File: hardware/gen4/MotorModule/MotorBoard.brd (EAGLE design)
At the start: 34 x 61.7 mm, 67 parts, among them IC1 XMEGA16A4A, M1O1 TEST_PT, M1O2 TEST_PT, M1O3 TEST_PT

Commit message: cleaned up a few things
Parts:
- R12, R13, R14: value 0 -> 240
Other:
- outline, holes or cut-outs redrawn
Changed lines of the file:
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@@
 <plain>
 <wire x1="-1" y1="-16.65875" x2="-1" y2="45" width="0.4064" layer="20"/>
-<wire x1="-1" y1="45" x2="33" y2="44.865" width="0.4064" layer="20"/>
-<wire x1="33" y1="44.865" x2="33" y2="-16.65875" width="0.4064" layer="20"/>
+<wire x1="-1" y1="45" x2="33" y2="45.02375" width="0.4064" layer="20"/>
+<wire x1="33" y1="45.02375" x2="33" y2="-16.65875" width="0.4064" layer="20"/>
 <wire x1="33" y1="-16.65875" x2="-1" y2="-16.65875" width="0.4064" layer="20"/>
 <text x="0.533125" y="45.761875" size="1.016" layer="21">Priorities:
 1. don't catch on fire
 2. play soccer</text>
+<dimension x1="33" y1="44.865" x2="33" y2="-16.65875" x3="46.19625" y3="14.103125" textsize="1.778" layer="20"/>
+<dimension x1="-1" y1="45" x2="33" y2="44.865" x3="16.074" y3="63.56980625" textsize="1.778" layer="20"/>
 </plain>
 <attributes>
@@
 <element name="R8" library="SparkFun-Resistors" package="0805" value="240" x="10.6875" y="32.8753125" rot="R180"/>
 <element name="R10" library="SparkFun-Resistors" package="0805" value="240" x="12.7" y="40.3225" rot="R180"/>
-<element name="R12" library="SparkFun-Resistors" package="0805" value="0" x="30.63875" y="22.70125" rot="R180"/>
-<element name="R13" library="SparkFun-Resistors" package="0805" value="0" x="28.2575" y="32.7025" rot="R180"/>
-<element name="R14" library="SparkFun-Resistors" package="0805" value="0" x="28.41625" y="40.9575" rot="R180"/>
+<element name="R12" library="SparkFun-Resistors" package="0805" value="240" x="30.63875" y="22.70125" rot="R180"/>
+<element name="R13" library="SparkFun-Resistors" package="0805" value="240" x="28.2575" y="32.7025" rot="R180"/>
+<element name="R14" library="SparkFun-Resistors" package="0805" value="240" x="28.41625" y="40.9575" rot="R180"/>
 <element name="R78" library="SparkFun-Resistors" package="0805" value="1k" x="21.74875" y="7.77875" rot="R90"/>
 <element name="R79" library="SparkFun-Resistors" package="0805" value="1k" x="21.74875" y="4.7625" rot="R90"/>

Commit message: motor board fix
final changes
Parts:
- R12, R13, R14: value 240 -> 0
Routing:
- net PWM1: track 49.3 -> 49.9 mm
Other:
- outline, holes or cut-outs redrawn

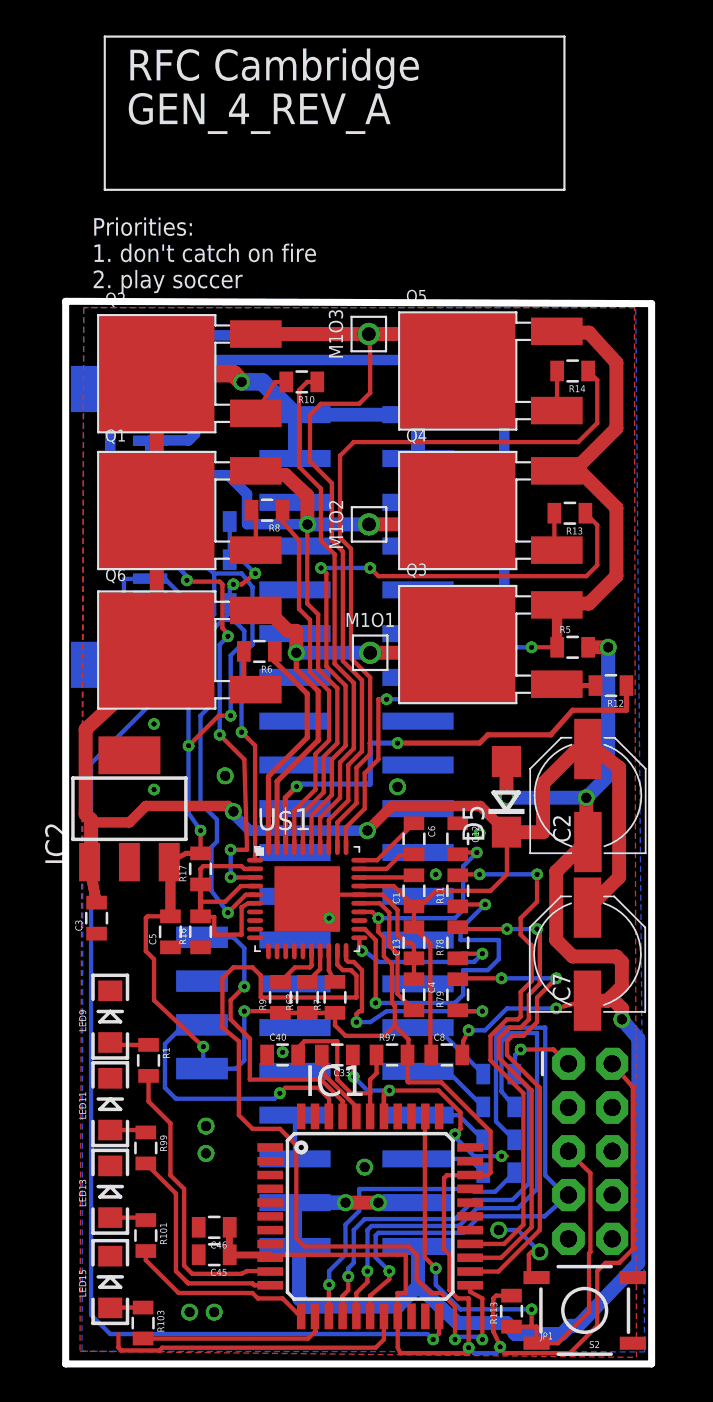
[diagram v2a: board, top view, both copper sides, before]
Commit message: motor and kicker fixes
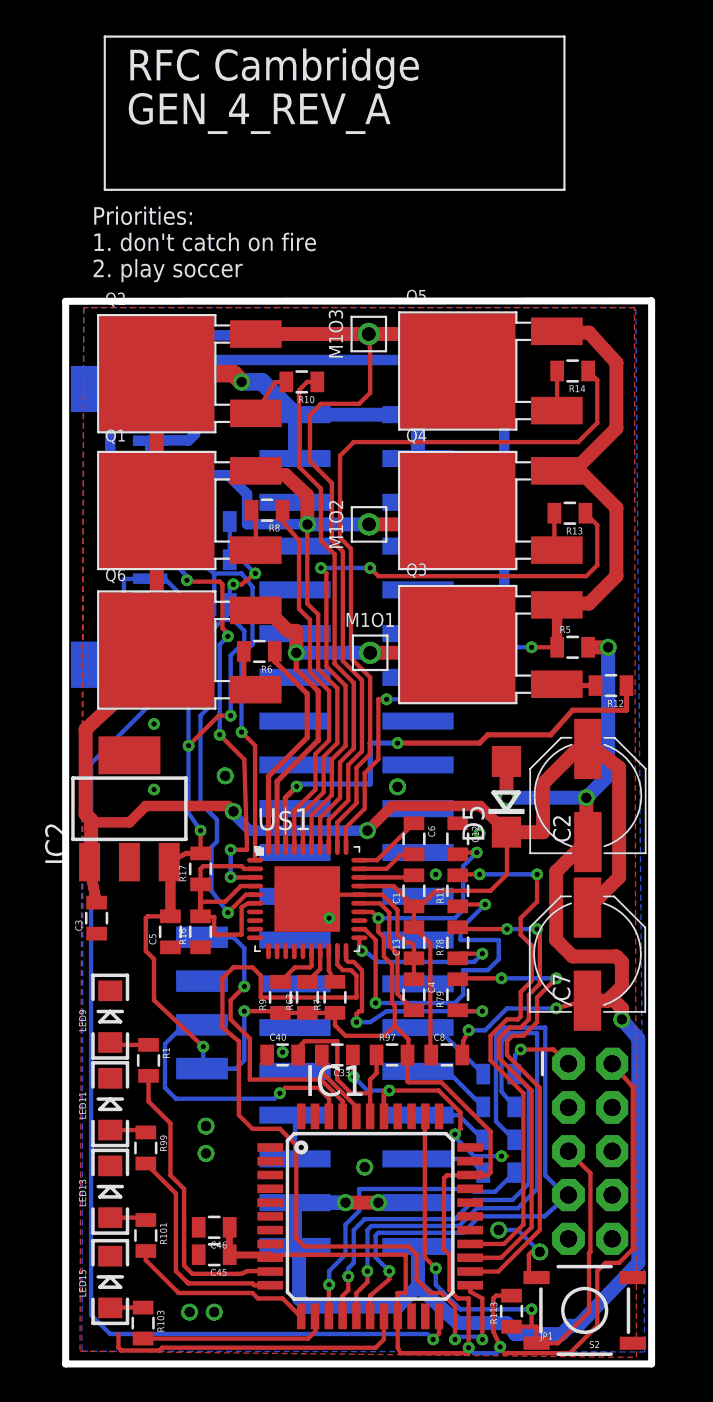
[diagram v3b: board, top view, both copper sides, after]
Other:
- outline, holes or cut-outs redrawn
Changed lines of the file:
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@@
 <plain>
 <wire x1="-1" y1="-16.65875" x2="-1" y2="45" width="0.4064" layer="20"/>
-<wire x1="-1" y1="45" x2="33" y2="44.865" width="0.4064" layer="20"/>
-<wire x1="33" y1="44.865" x2="33" y2="-16.65875" width="0.4064" layer="20"/>
+<wire x1="-1" y1="45" x2="33" y2="45.02375" width="0.4064" layer="20"/>
+<wire x1="33" y1="45.02375" x2="33" y2="-16.65875" width="0.4064" layer="20"/>
 <wire x1="33" y1="-16.65875" x2="-1" y2="-16.65875" width="0.4064" layer="20"/>
-<text x="0.533125" y="45.761875" size="1.016" layer="21">Priorities:
+<text x="0.533125" y="46.396875" size="1.016" layer="21">Priorities:
 1. don't catch on fire
 2. play soccer</text>

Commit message: motor layout stuff
idea: maybe moving some more stuff to the bottom would be beneficial
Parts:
- R12, R13, R14: value 0 -> 240
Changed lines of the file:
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@@
 <element name="R8" library="SparkFun-Resistors" package="0805" value="240" x="10.6875" y="32.8753125" rot="R180"/>
 <element name="R10" library="SparkFun-Resistors" package="0805" value="240" x="12.7" y="40.3225" rot="R180"/>
-<element name="R12" library="SparkFun-Resistors" package="0805" value="0" x="30.63875" y="22.70125" rot="R180"/>
-<element name="R13" library="SparkFun-Resistors" package="0805" value="0" x="28.2575" y="32.7025" rot="R180"/>
-<element name="R14" library="SparkFun-Resistors" package="0805" value="0" x="28.41625" y="40.9575" rot="R180"/>
+<element name="R12" library="SparkFun-Resistors" package="0805" value="240" x="30.63875" y="22.70125" rot="R180"/>
+<element name="R13" library="SparkFun-Resistors" package="0805" value="240" x="28.2575" y="32.7025" rot="R180"/>
+<element name="R14" library="SparkFun-Resistors" package="0805" value="240" x="28.41625" y="40.9575" rot="R180"/>
 <element name="R78" library="SparkFun-Resistors" package="0805" value="1k" x="21.74875" y="7.77875" rot="R90"/>
 <element name="R79" library="SparkFun-Resistors" package="0805" value="1k" x="21.74875" y="4.7625" rot="R90"/>

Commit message: passes erc
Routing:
- net N$22: track 15.7 -> 14.8 mm
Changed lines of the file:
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@@
 <wire x1="9.9925" y1="10.06875" x2="9.5925" y2="10.06875" width="0.254" layer="1"/>
 <wire x1="9.5925" y1="10.06875" x2="9.2075" y2="9.8425" width="0.254" layer="1"/>
-<wire x1="9.2075" y1="9.8425" x2="9.2075" y2="8.255" width="0.254" layer="1"/>
-<wire x1="9.2075" y1="8.255" x2="7.62" y2="8.255" width="0.254" layer="1"/>
-<wire x1="7.62" y1="8.255" x2="7.62" y2="9.275" width="0.254" layer="1"/>
+<wire x1="9.2075" y1="9.8425" x2="9.04875" y2="8.5725" width="0.254" layer="1"/>
+<wire x1="9.04875" y1="8.5725" x2="7.77875" y2="8.5725" width="0.254" layer="1"/>
+<wire x1="7.77875" y1="8.5725" x2="7.62" y2="9.275" width="0.254" layer="1"/>
 <wire x1="9.9925" y1="12.06875" x2="9.36625" y2="12.065" width="0.254" layer="1"/>
 <wire x1="9.36625" y1="12.065" x2="9.2075" y2="12.22375" width="0.254" layer="1"/>

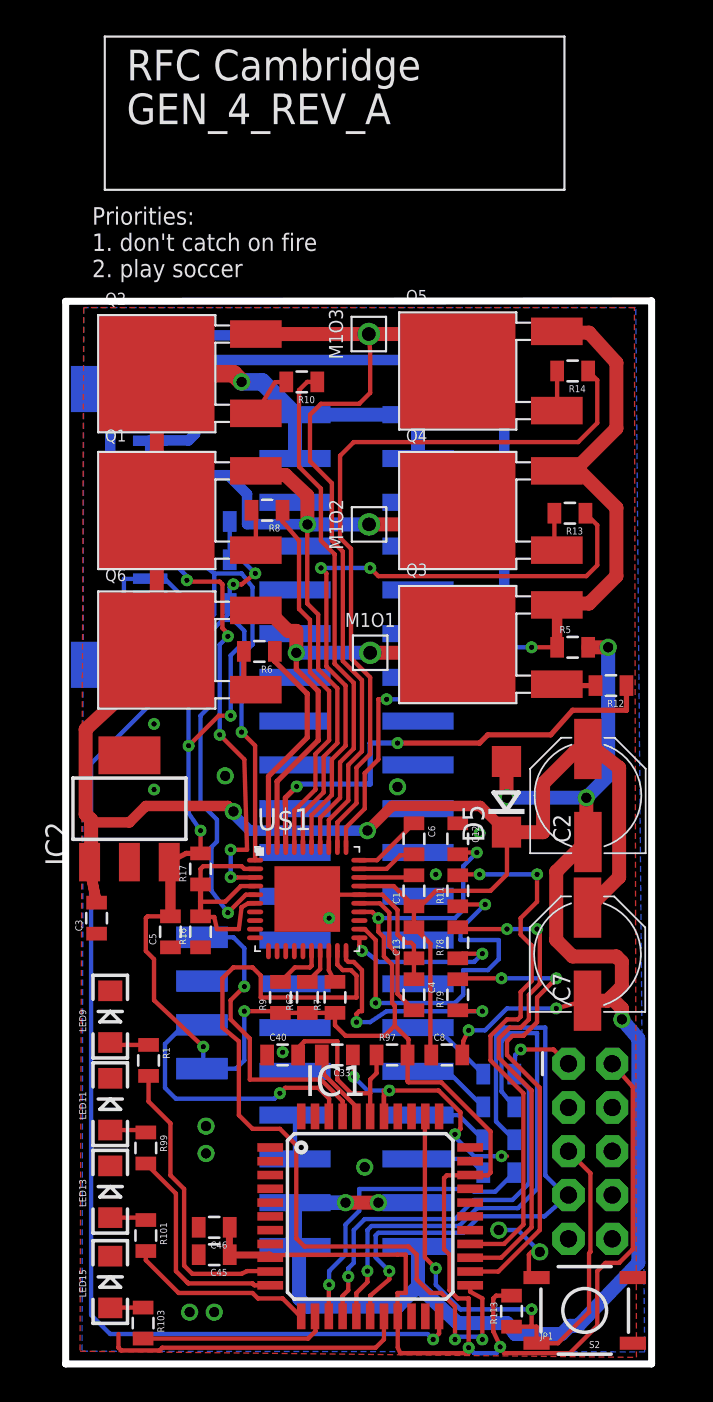
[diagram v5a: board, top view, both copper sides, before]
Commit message: motorboard and kickerboard ordered thanks caffeine
fixes include: overlaps, adding mounting points panelizing and
gerberfiles,, and clearance issues.
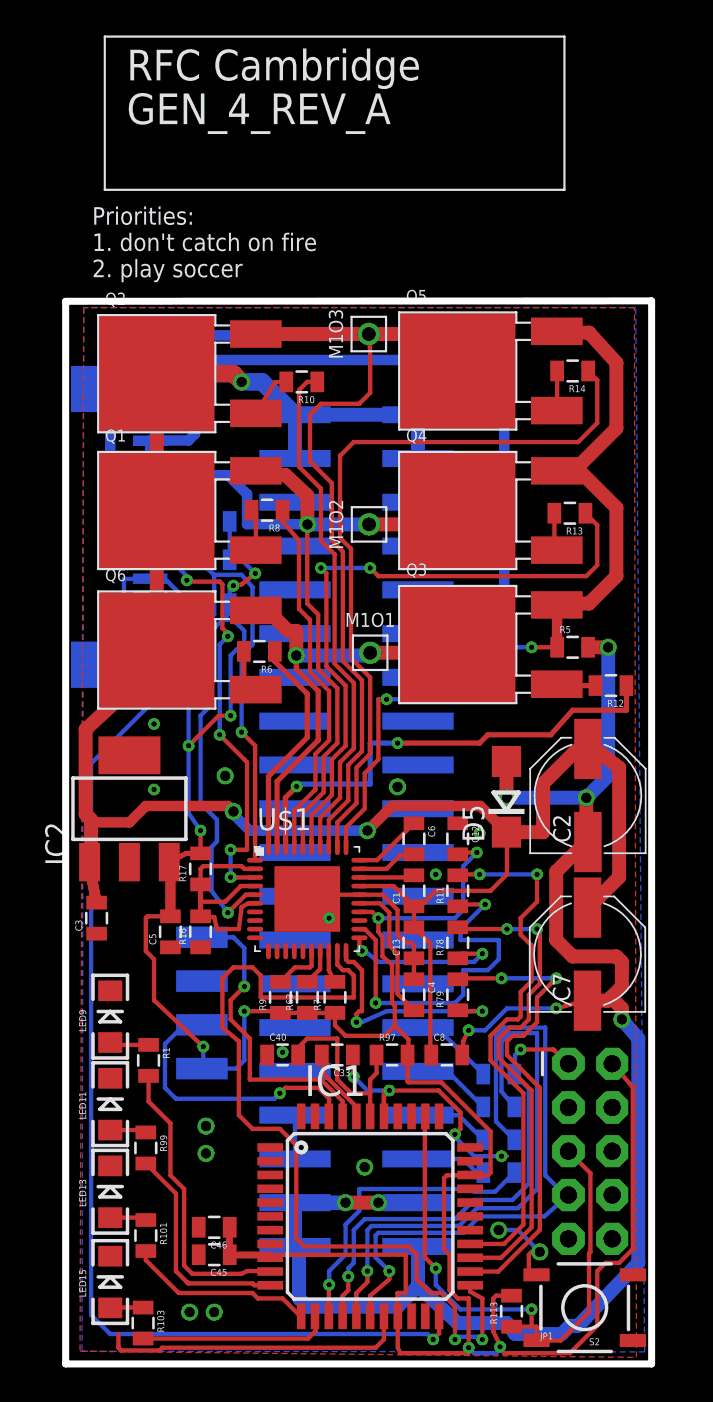
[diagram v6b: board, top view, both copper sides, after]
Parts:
- moved S2 0.16 mm to (29.1, -13.4)

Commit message: fixing motorboard
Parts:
- removed JP1: (no value), SparkFun-Connectors:2X5-SHROUDED-NS
- removed U$2: MOTORCON, gen3:GEN3CON
- added JP2: (no value), pinhead:2X03
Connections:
- new net DATA: IC1.34, JP2.1
- net 3.3V: now also JP2.2, JP3.23; no longer JP1.2, U$2.1
- net GND: now also JP2.6, JP3.15; no longer JP1.10, JP1.4, JP1.6, JP1.8, U$2.5
- net M1H1: now also JP3.19; no longer U$2.3
- net M1H2: now also JP3.17; no longer U$2.4
- net M1H3: now also JP3.21; no longer U$2.2
- net M1O1: now also JP3.10, JP3.9; no longer U$2.10, U$2.11
- net M1O2: now also JP3.11, JP3.12; no longer U$2.8, U$2.9
- net M1O3: now also JP3.13, JP3.14; no longer U$2.6, U$2.7
- net MOSI: no longer JP1.1
- net RESET: now also JP2.5; no longer JP1.5
- net SCK: no longer JP1.7
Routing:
- net M1O1: track 77.0 -> 37.6 mm
- net M1O3: track 76.8 -> 91.4 mm
- net M1H1: track 31.5 -> 23.0 mm
- net M1H3: track 28.1 -> 35.7 mm
- net 3.3V: track 159.9 -> 154.5 mm
- net MOSI: track 28.0 -> 23.3 mm, vias 2 -> 1
- net M1O2: track 49.0 -> 51.9 mm
- net M1H2: track 28.3 -> 26.3 mm
- net SCK: track 37.6 -> 35.7 mm

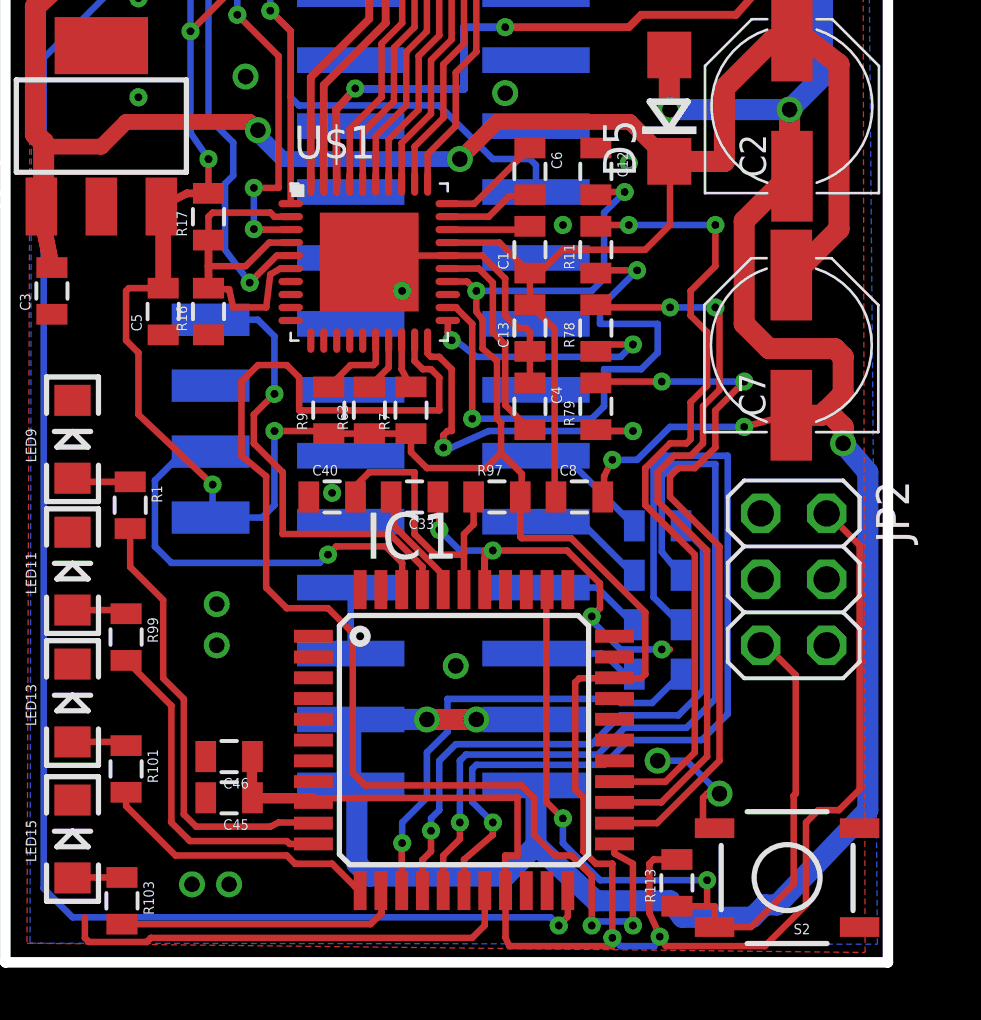
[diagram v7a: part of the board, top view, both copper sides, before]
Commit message: motor board 5v error updated
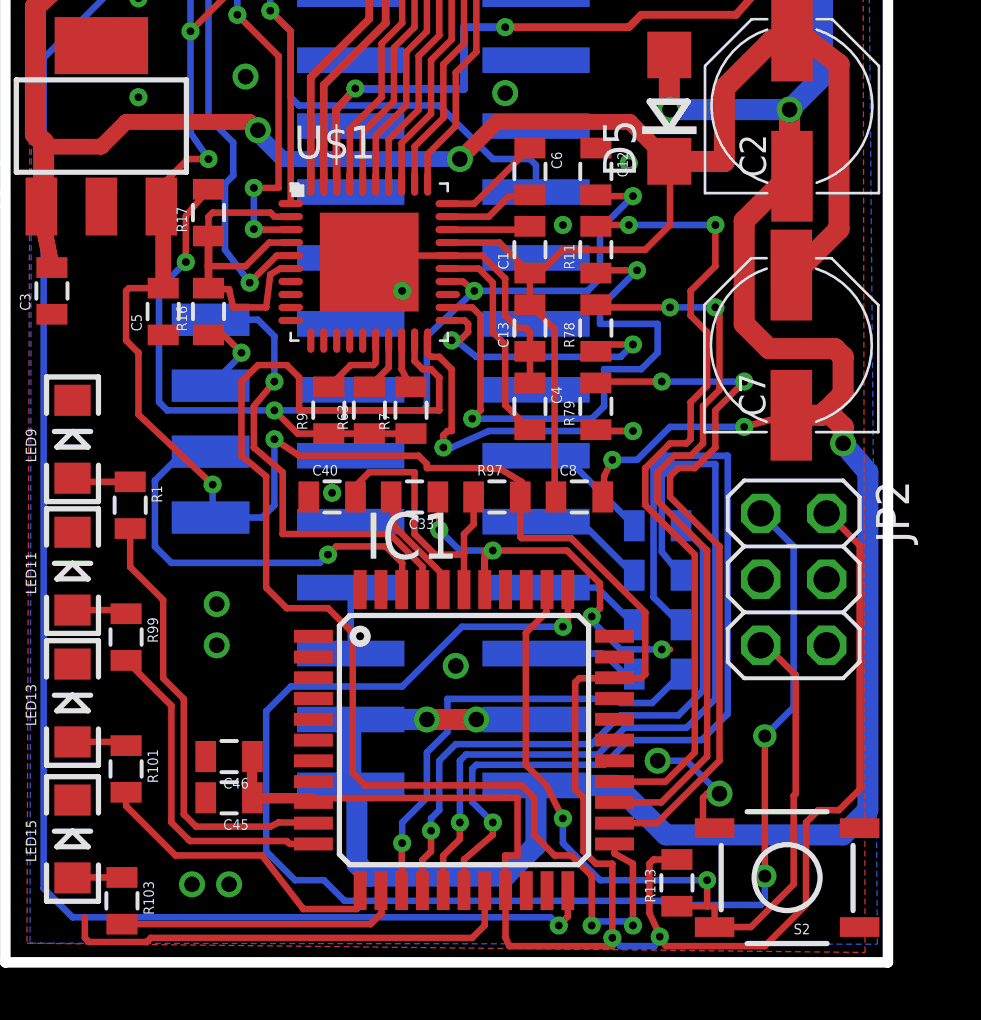
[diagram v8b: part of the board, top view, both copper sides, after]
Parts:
- moved R17 0.16 mm to (6.83, 12.2)
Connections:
- new net 5V: C12.2, R17.2, R63.1, R7.1, R9.1, U$1.24
- net 3.3V: no longer C12.2, R17.2, R63.1, R7.1, R9.1, U$1.24
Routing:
- net DATA: track 0.00 -> 55.8 mm, vias 0 -> 3
- net 5V: track 0.00 -> 41.7 mm, vias 0 -> 4
- net 3.3V: track 154.5 -> 134.9 mm, vias 11 -> 9
- net GND: track 58.8 -> 62.1 mm, vias 19 -> 20
- net 12VGND: track 104.0 -> 102.6 mm
- net GLED3: track 10.9 -> 12.3 mm
- net N$98: track 9.74 -> 10.9 mm
- net N$32: track 21.5 -> 22.1 mm
